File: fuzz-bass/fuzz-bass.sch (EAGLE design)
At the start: 16 parts, among them Q1 2N4036, Q2 2N4036

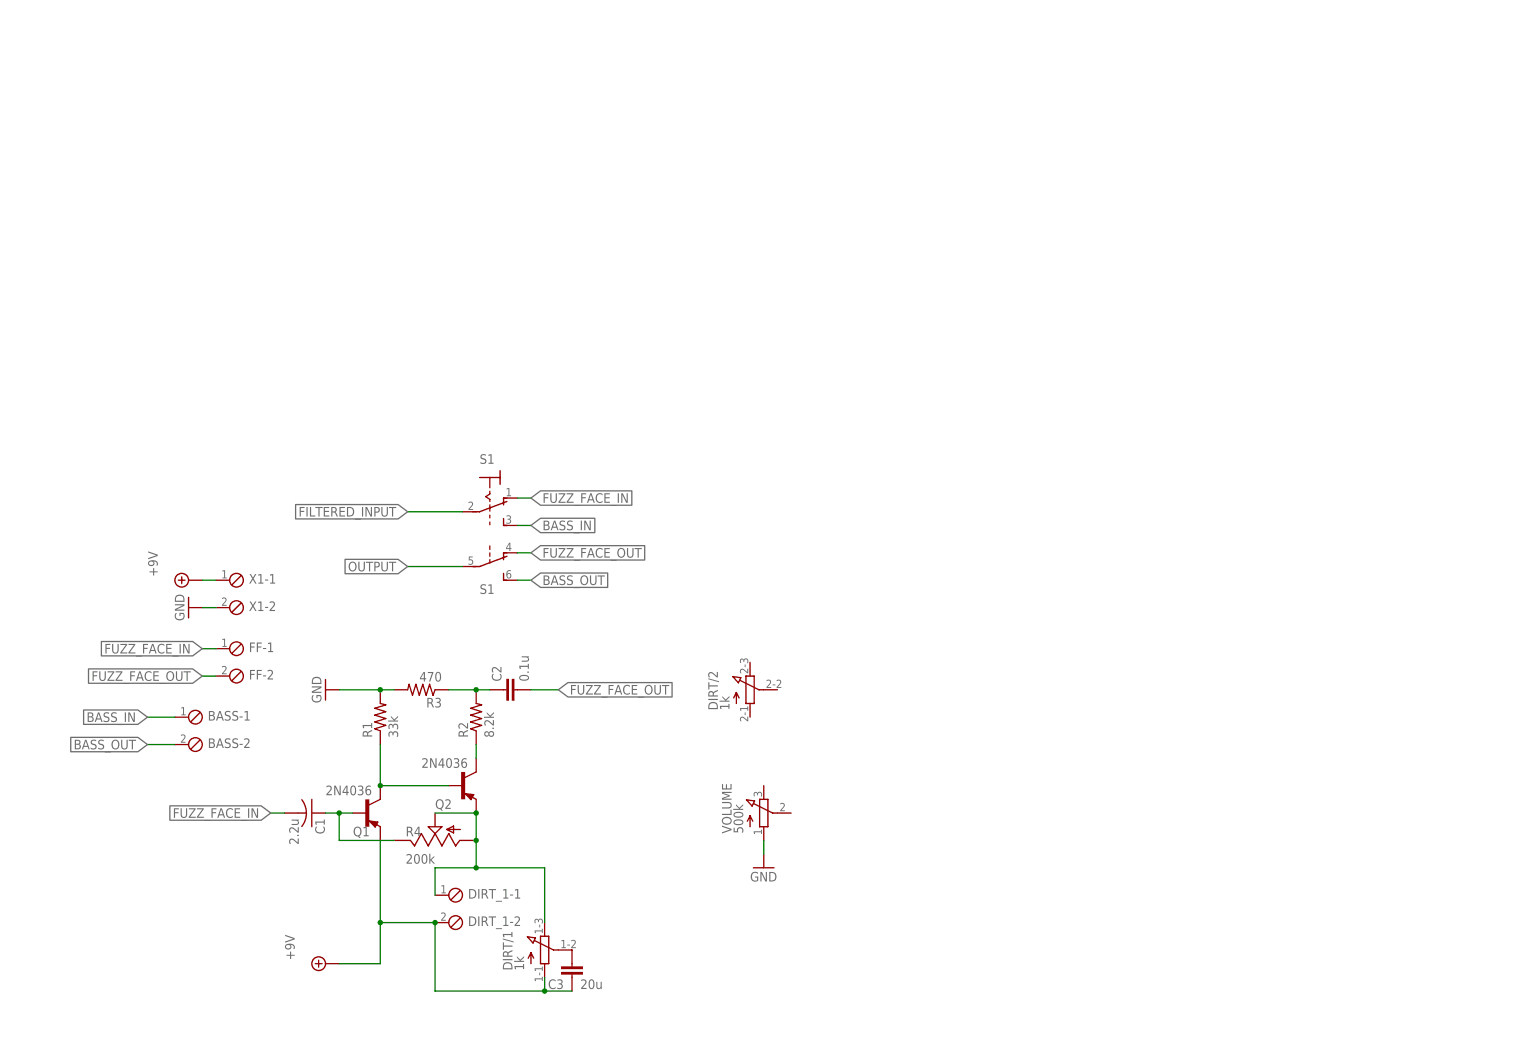
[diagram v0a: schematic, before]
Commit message: Add bass section to fuzz bass.
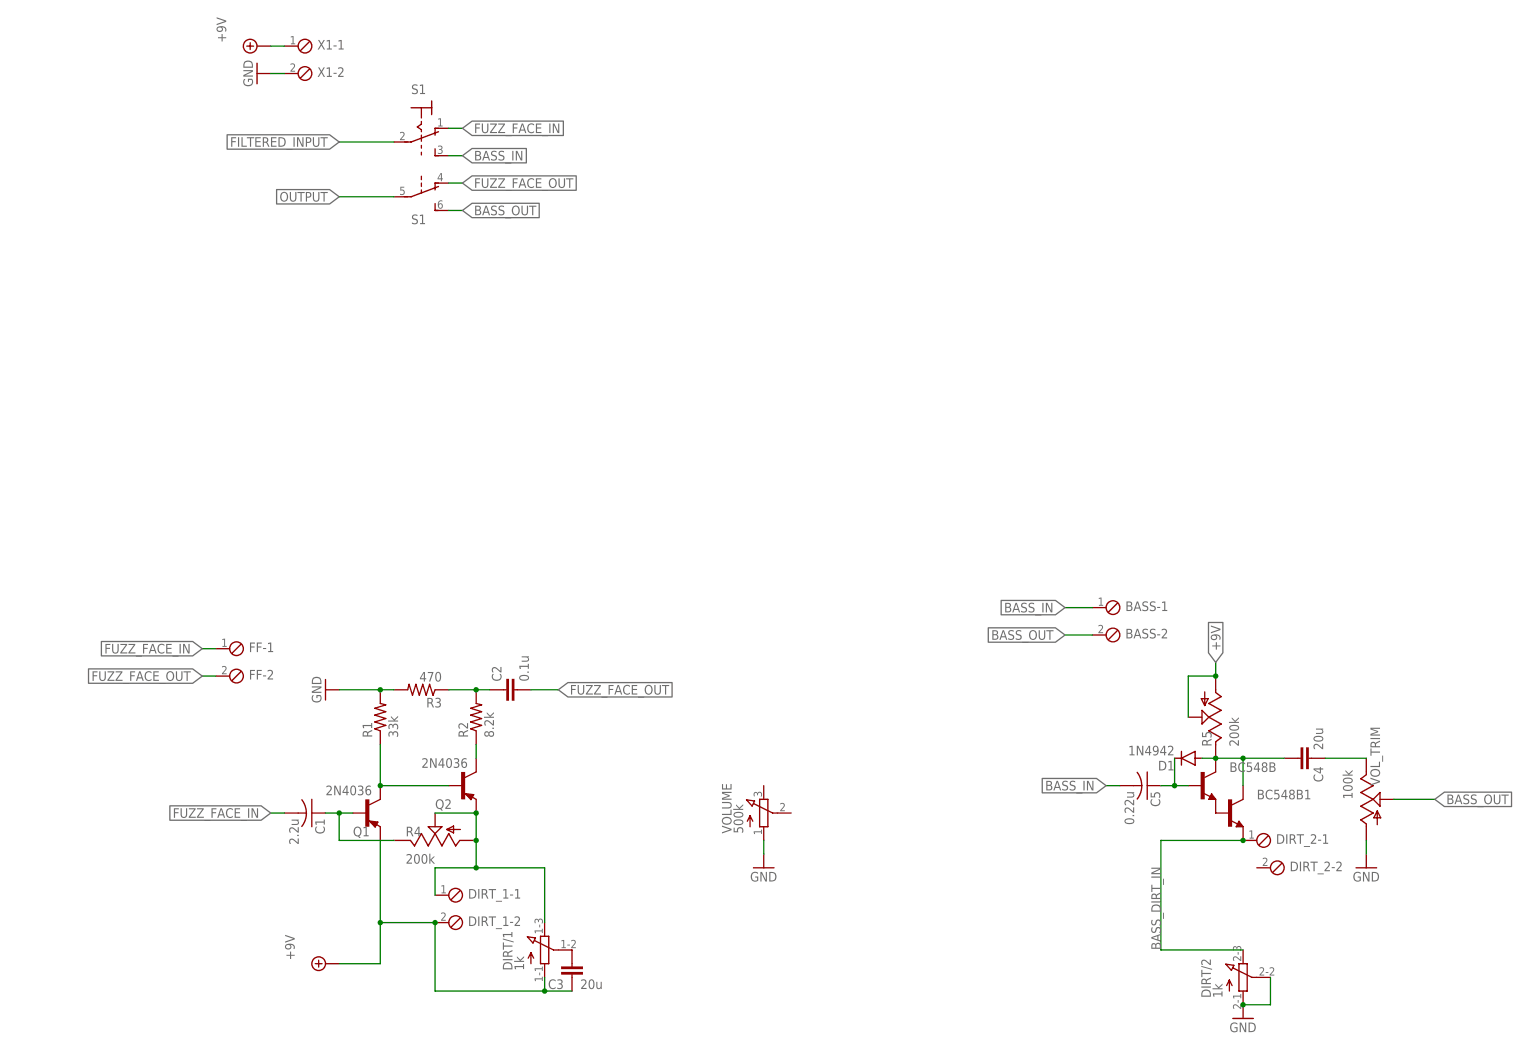
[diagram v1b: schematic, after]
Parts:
- added BC548B, BC548B1: (no value), transistor:-NPN-TO92L
- added C4: 20u, rcl:C-EU025-030X050
- added C5: 0.22u, adafruit:C-US025-050X050
- added D1: 1N4942, diode:1N4942
- added DIRT_2: (no value), con-phoenix-254:MPT2
- added R5: 200k, pot:TRIM_US-RJ9W
- added VOL_TRIM: 100k, pot:TRIM_US-RJ9W
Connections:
- new net BASS_DIRT_IN: BC548B1.E, DIRT/2.E, DIRT_2-1.1
- new net N$11: BC548B.B, C5.1, D1.C
- new net N$12: C4.1, VOL_TRIM.E
- new net N$7: BC548B.E, BC548B1.B
- new net N$8: BC548B.C, BC548B1.C, C4.2, D1.A, R5.E
- net +9V: now also R5.A, R5.S
- net BASS_IN: now also C5.2
- net BASS_OUT: now also VOL_TRIM.S
- net GND: now also DIRT/2.A, DIRT/2.S, VOL_TRIM.A
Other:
- moved on the sheet: BASS-1, BASS-2, DIRT/2, S1, X1-1, X1-2

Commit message: Updates to fuzz-bass.
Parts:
- added C6: 0.22u, rcl:C-EU050-024X044
- added C7: 0.001u, rcl:C-EU050-024X044
- added G1: AB9V, battery:AB9V
- added INPUT_JACK, OUTPUT_JACK1: JACK6.35MM, jack-eagle:JACK6.35MM
- added J1: (no value), con-jack:DCJ0303
- added LED1: (no value), led:LED3MM
- added R6: 100k, rcl:R-US_0204/7
- added R7: 1M, rcl:R-US_0204/7
- added S3: 3PDT, switch:3PDT
- added VOLUME1: 500k, pot:3RP/1610N
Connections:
- net N$2 renamed FACE_DIRT_IN
- removed net FILTERED_INPUT: S11.P
- new net FUZZED_OUTPUT: S3.S3, VOLUME.S
- new net INPUT: C7.1, INPUT_JACK.TIP, R7.2, S3.P1, VOLUME1.A
- new net N$10: LED1.A, R6.2
- new net N$13: C6.1, VOLUME1.E, VOLUME1.S
- new net N$14: S3.O1, S3.O3
- new net N$15: G1.-, INPUT_JACK.RING
- new net N$16: S12.P, VOLUME.E
- new net N$9: R6.1, S3.S2
- new net TONE_INPUT: S3.S1
- new net TONE_OUTPUT: C6.2, C7.2, S11.P
- net +9V: now also G1.+, S3.P2
- net GND: now also INPUT_JACK.SLEEVE, INPUT_JACK.SLEEVE-DISCON, LED1.C, OUTPUT_JACK1.SLEEVE, OUTPUT_JACK1.SLEEVE-DISCON, R7.1
- net OUTPUT: now also OUTPUT_JACK1.TIP, S3.P3; no longer S12.P
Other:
- moved on the sheet: C1, C2, C3, DIRT/1, DIRT_1-1, DIRT_1-2, FF-1, FF-2, Q1, Q2, R1, R2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
